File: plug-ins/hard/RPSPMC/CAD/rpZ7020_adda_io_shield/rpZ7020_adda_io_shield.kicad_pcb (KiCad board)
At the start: 4 copper layers, 70.6 x 94.5 mm, 36 parts, among them J1 Samtec_ASP-134486-01, J2 Conn_01x03_Socket, J2-FMC-RP1 Conn_02x20, J2-PWR3 Conn_01x03_Pin, J3-FMC-POWER1 Conn_02x06_Odd_Even, J3-PWR12 Conn_01x02_Pin, J4-FMC-AUX1 Conn_02x06_Odd_Even

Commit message: work on SPI
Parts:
- added U1: TC7QPB9306FK, Package_SO:TSSOP-14_4.4x5mm_P0.65mm, F.Cu at (94.4, 122.8)
- added U2: TC7QPB9306FK, Package_SO:TSSOP-14_4.4x5mm_P0.65mm, F.Cu at (100.2, 122.8)
- added U3: TC7QPB9306FK, Package_SO:TSSOP-14_4.4x5mm_P0.65mm, F.Cu at (106.0, 122.8)

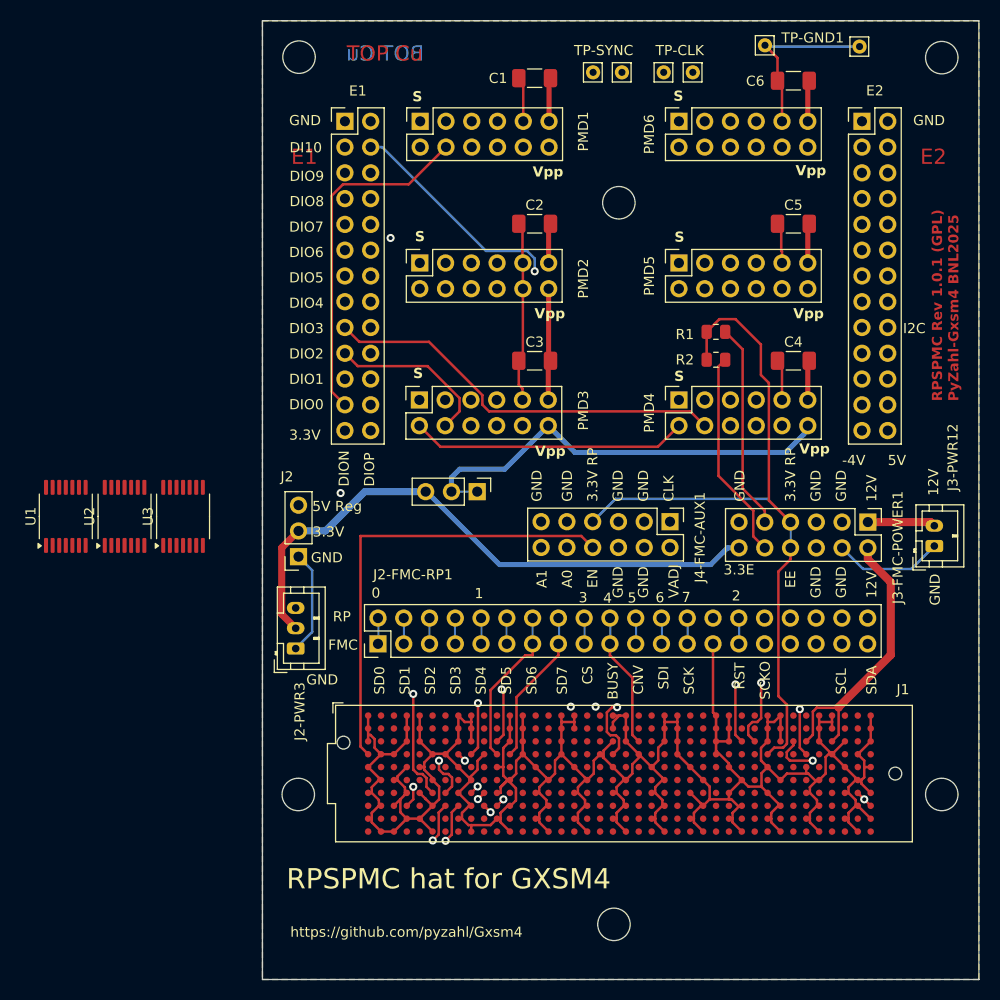
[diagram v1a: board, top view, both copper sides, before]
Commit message: updated PCB: Vadj --- 3.3V
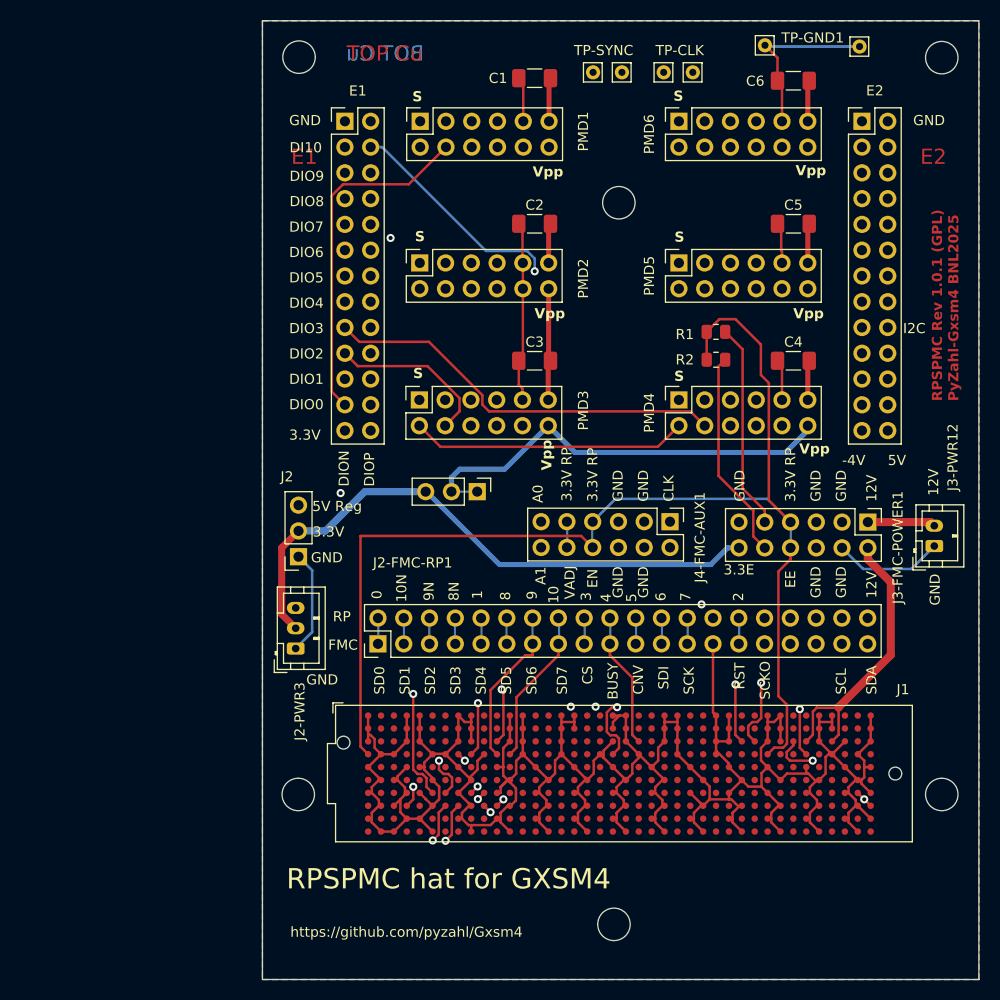
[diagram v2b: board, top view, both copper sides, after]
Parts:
- removed U1, U2, U3: TC7QPB9306FK, Package_SO:TSSOP-14_4.4x5mm_P0.65mm
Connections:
- J4-FMC-AUX1 pad 10: A0 EE -> VADJ
- J4-FMC-AUX1 pad 11: GND -> A0 EE
- J4-FMC-AUX1 pad 2: VADJ -> unconnected-(J4-FMC-AUX1-Pin_2-Pad2)
- J4-FMC-AUX1 pad 9: GND -> RP 3.3V
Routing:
- net GND: track 552.4 -> 533.1 mm
- net 5V USB: track 11.4 -> 22.5 mm
- net VADJ: track 35.3 -> 45.3 mm, vias 1 -> 2
- net A0 EE: track 46.4 -> 51.0 mm
- net RP 3.3V: track 90.1 -> 92.7 mm
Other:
- board text added: "10"
- board text added: "10N"
- board text added: "8"
- board text added: "8N"
- board text added: "9"
- board text added: "9N"
